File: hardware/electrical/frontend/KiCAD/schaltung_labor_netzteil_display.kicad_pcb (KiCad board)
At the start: 2 copper layers, 99.1 x 95.2 mm, 15 parts, among them J1 V_psu +, J10 SW+, J11 SW-, J2 V_psu -, J3 V_out +, J4 V_out -, J5 +5V, J6 GND / V_in -, J7 PWM, J8 U_in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

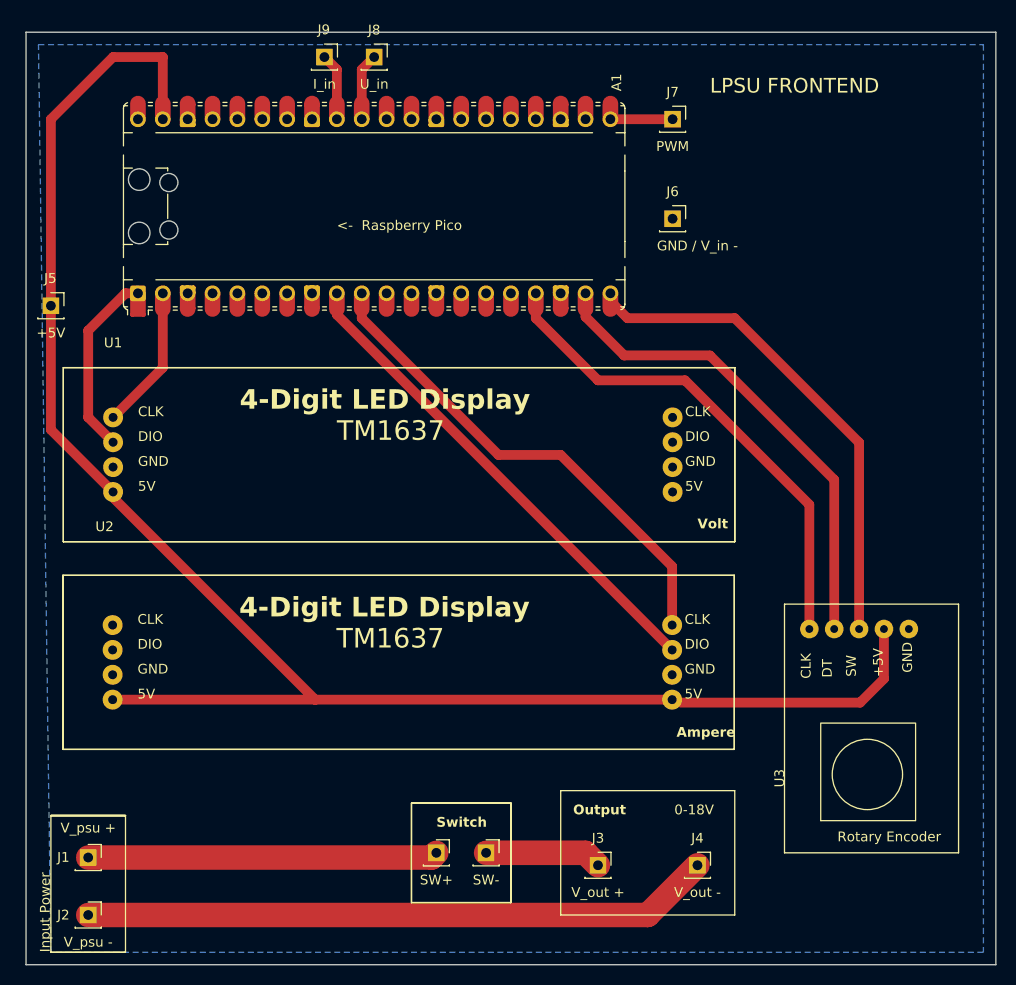
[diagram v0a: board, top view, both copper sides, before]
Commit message: Updated PCBs; added Bleed Resistor and fixed Frontend GND connections
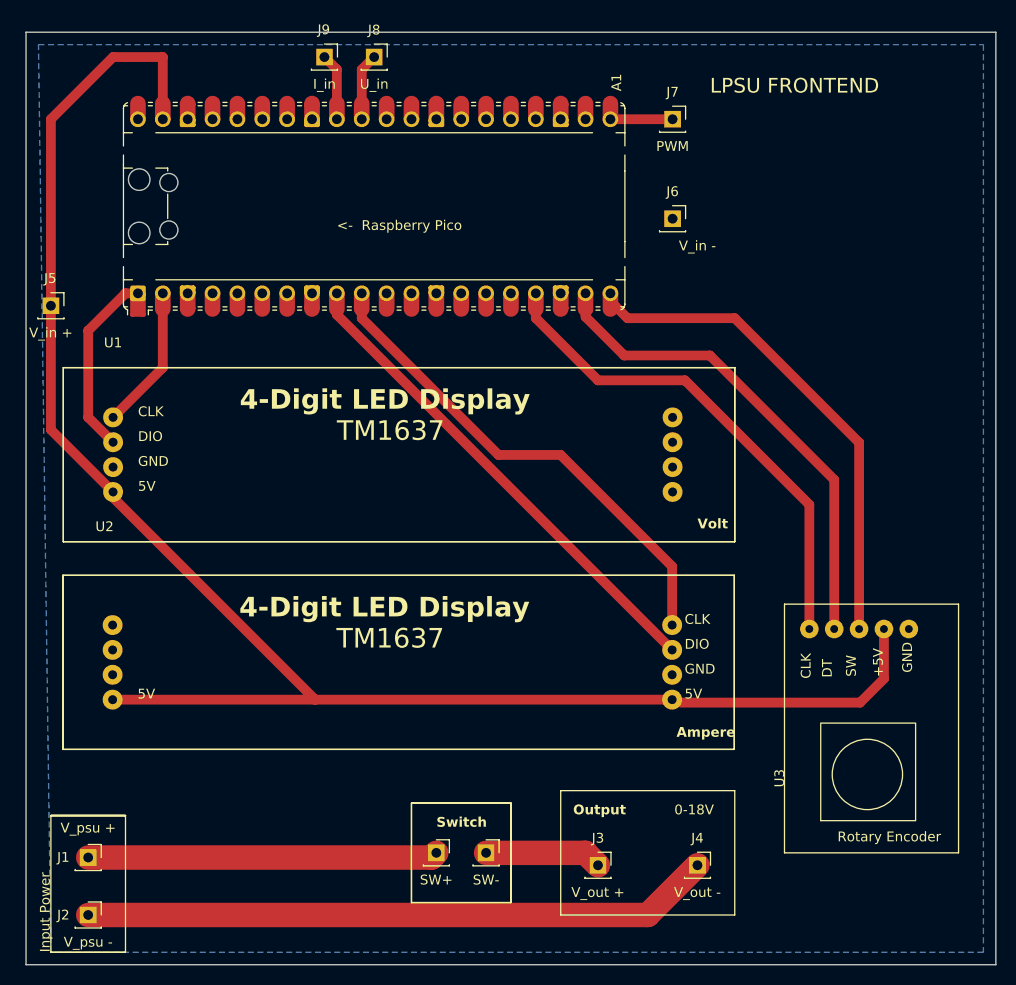
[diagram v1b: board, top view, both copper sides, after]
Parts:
- J5: value +5V -> V_in +
- J6: value GND / V_in - -> V_in -
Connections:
- A1 pad 13: Net-(A1-GND-Pad13) -> GND
- A1 pad 18: Net-(A1-GND-Pad13) -> GND
- A1 pad 23: Net-(A1-GND-Pad13) -> GND
- A1 pad 28: Net-(A1-GND-Pad13) -> GND
- A1 pad 3: Net-(A1-GND-Pad13) -> GND
- A1 pad 33: unconnected-(A1-AGND-Pad33) -> GND
- A1 pad 38: Net-(A1-GND-Pad13) -> GND
- A1 pad 8: Net-(A1-GND-Pad13) -> GND
